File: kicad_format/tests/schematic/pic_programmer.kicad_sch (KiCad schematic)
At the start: 56 parts, among them J1 DB9-FEMAL, P1 CONN_2, P101 CONN_1, P102 CONN_1, P103 CONN_1, P104 CONN_1, P105 CONN_1, P106 CONN_1, Q1 BC237, Q2 BC307, Q3 BC307, U2 74HC125, U3 7805, U4 LT1373

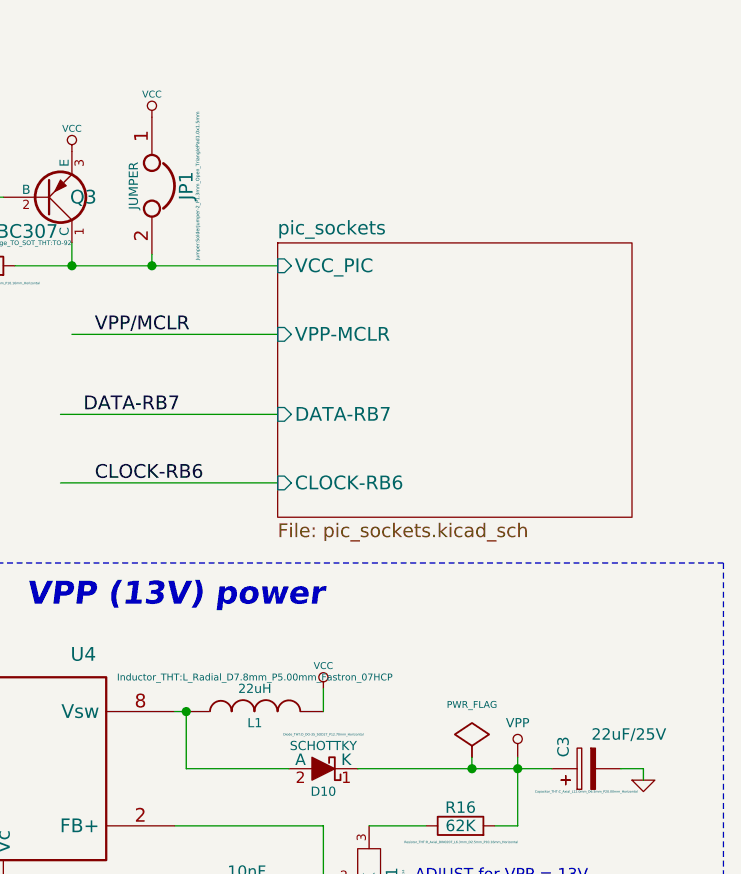
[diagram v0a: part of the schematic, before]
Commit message: Add serialization context and support most modern kicad file idiosyncrasies
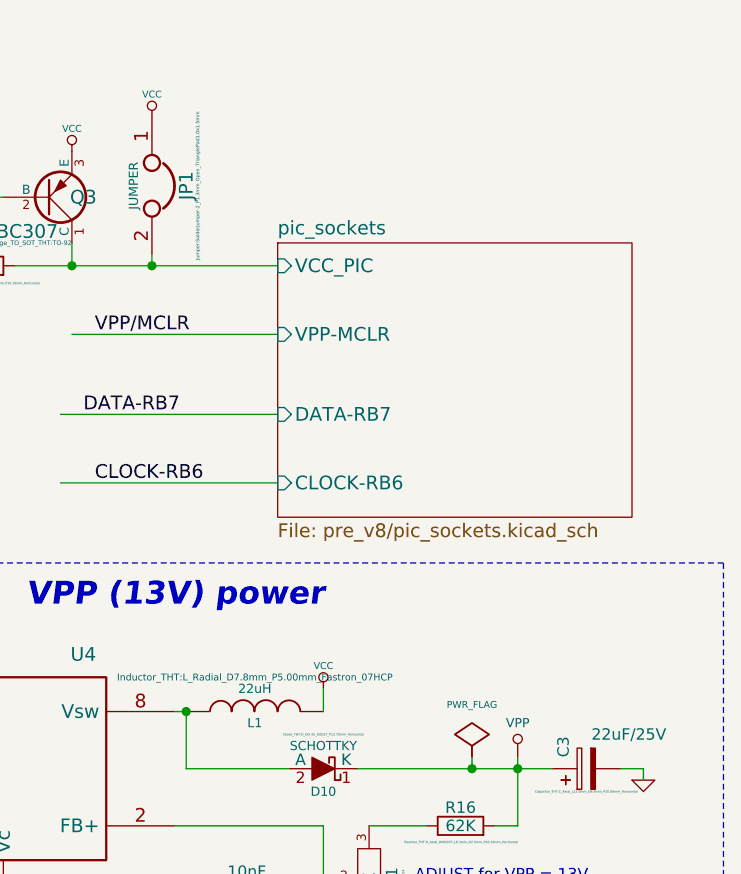
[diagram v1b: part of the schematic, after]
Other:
- sheet pic_sockets: file pic_sockets.kicad_sch -> pre_v8/pic_sockets.kicad_sch
